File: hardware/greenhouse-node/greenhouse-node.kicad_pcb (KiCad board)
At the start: 2 copper layers, 90.2 x 69.8 mm, 49 parts, among them J1 Conn_01x12_Male, J2 Conn_01x02_Male, J3 Conn_01x02_Male, J4 Conn_01x02_Male, J5 Conn_01x04_Male, J6 RX_PinHeader_1x04_P2.54mm, J7 TX_PinHeader_1x04_P2.54mm, J8 Conn_01x02_Male, Q1 BC549C, Q2 BC549C, Q3 BC549C, Q4 IRF9530N, Q5 IRF530N, Q6 IRF9530N, Q7 IRF530N, Q8 BC549C, Q9 BC549C, U1 ATtiny84A-P, U2 L7805, U3 74HC595

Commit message: Tweak net positions
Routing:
- net /SR_RCLK: track 66.9 -> 68.4 mm
- net /SR_CLK: track 64.8 -> 65.6 mm
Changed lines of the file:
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@@
   (segment (start 139.446 92.837) (end 138.43 91.821) (width 0.25) (layer "F.Cu") (net 13))
   (segment (start 145.669 92.837) (end 139.446 92.837) (width 0.25) (layer "F.Cu") (net 13))
+  (segment (start 135.255 87.503) (end 135.255 72.0725) (width 0.25) (layer "B.Cu") (net 13))
+  (segment (start 134.511254 62.738) (end 137.541 62.738) (width 0.25) (layer "B.Cu") (net 13))
+  (segment (start 136.017 88.265) (end 135.255 87.503) (width 0.25) (layer "B.Cu") (net 13))
+  (segment (start 131.953 65.296254) (end 134.511254 62.738) (width 0.25) (layer "B.Cu") (net 13))
+  (segment (start 139.71 88.265) (end 136.017 88.265) (width 0.25) (layer "B.Cu") (net 13))
+  (segment (start 137.541 62.738) (end 140.723 59.556) (width 0.25) (layer "B.Cu") (net 13))
+  (segment (start 131.953 68.7705) (end 131.953 65.296254) (width 0.25) (layer "B.Cu") (net 13))
+  (segment (start 140.723 59.556) (end 140.723 58.022) (width 0.25) (layer "B.Cu") (net 13))
   (segment (start 135.255 72.0725) (end 131.953 68.7705) (width 0.25) (layer "B.Cu") (net 13))
-  (segment (start 131.953 65.296254) (end 134.511254 62.738) (width 0.25) (layer "B.Cu") (net 13))
-  (segment (start 137.541 62.738) (end 140.723 59.556) (width 0.25) (layer "B.Cu") (net 13))
-  (segment (start 138.557 88.265) (end 135.255 84.963) (width 0.25) (layer "B.Cu") (net 13))
-  (segment (start 131.953 68.7705) (end 131.953 65.296254) (width 0.25) (layer "B.Cu") (net 13))
-  (segment (start 135.255 84.963) (end 135.255 72.0725) (width 0.25) (layer "B.Cu") (net 13))
-  (segment (start 139.71 88.265) (end 138.557 88.265) (width 0.25) (layer "B.Cu") (net 13))
-  (segment (start 134.511254 62.738) (end 137.541 62.738) (width 0.25) (layer "B.Cu") (net 13))
-  (segment (start 140.723 59.556) (end 140.723 58.022) (width 0.25) (layer "B.Cu") (net 13))
+  (segment (start 139.319 94.107) (end 139.319 99.568) (width 0.25) (layer "B.Cu") (net 14))
+  (segment (start 132.09 90.805) (end 133.731 90.805) (width 0.25) (layer "B.Cu") (net 14))
+  (segment (start 145.542 101.473) (end 147.955 103.886) (width 0.25) (layer "B.Cu") (net 14))
   (segment (start 147.955 103.886) (end 147.955 105.41) (width 0.25) (layer "B.Cu") (net 14))
-  (segment (start 132.09 90.805) (end 133.731 90.805) (width 0.25) (layer "B.Cu") (net 14))
-  (segment (start 141.224 101.473) (end 145.542 101.473) (width 0.25) (layer "B.Cu") (net 14))
   (segment (start 135.723 59.476) (end 135.723 58.022) (width 0.25) (layer "B.Cu") (net 14))
-  (segment (start 133.731 90.805) (end 136.779 90.805) (width 0.25) (layer "B.Cu") (net 14))
   (segment (start 139.319 99.568) (end 141.224 101.473) (width 0.25) (layer "B.Cu") (net 14))
   (segment (start 130.683 64.516) (end 135.723 59.476) (width 0.25) (layer "B.Cu") (net 14))
   (segment (start 133.731 90.805) (end 133.731 72.415701) (width 0.25) (layer "B.Cu") (net 14))
   (segment (start 133.731 72.415701) (end 130.683 69.367701) (width 0.25) (layer "B.Cu") (net 14))
+  (segment (start 133.731 90.805) (end 136.017 90.805) (width 0.25) (layer "B.Cu") (net 14))
   (segment (start 130.683 69.367701) (end 130.683 64.516) (width 0.25) (layer "B.Cu") (net 14))
-  (segment (start 139.319 93.345) (end 139.319 99.568) (width 0.25) (layer "B.Cu") (net 14))
-  (segment (start 145.542 101.473) (end 147.955 103.886) (width 0.25) (layer "B.Cu") (net 14))
-  (segment (start 136.779 90.805) (end 139.319 93.345) (width 0.25) (layer "B.Cu") (net 14))
+  (segment (start 136.017 90.805) (end 139.319 94.107) (width 0.25) (layer "B.Cu") (net 14))
+  (segment (start 141.224 101.473) (end 145.542 101.473) (width 0.25) (layer "B.Cu") (net 14))
   (segment (start 144.907 90.805) (end 155.575 101.473) (width 0.25) (layer "F.Cu") (net 15))
   (segment (start 155.575 101.473) (end 155.575 105.41) (width 0.25) (layer "F.Cu") (net 15))
   (segment (start 139.71 90.805) (end 144.907 90.805) (width 0.25) (layer "F.Cu") (net 15))
+  (segment (start 134.493 72.263) (end 131.318 69.088) (width 0.25) (layer "B.Cu") (net 15))
+  (segment (start 138.223 59.389) (end 138.223 58.022) (width 0.25) (layer "B.Cu") (net 15))
+  (segment (start 131.318 69.088) (end 131.318 64.897) (width 0.25) (layer "B.Cu") (net 15))
+  (segment (start 131.318 64.897) (end 134.493 61.722) (width 0.25) (layer "B.Cu") (net 15))
   (segment (start 135.89 61.722) (end 138.223 59.389) (width 0.25) (layer "B.Cu") (net 15))
-  (segment (start 131.318 69.088) (end 131.318 64.897) (width 0.25) (layer "B.Cu") (net 15))
-  (segment (start 134.493 72.263) (end 131.318 69.088) (width 0.25) (layer "B.Cu") (net 15))
-  (segment (start 131.318 64.897) (end 134.493 61.722) (width 0.25) (layer "B.Cu") (net 15))
-  (segment (start 139.71 90.805) (end 138.557 90.805) (width 0.25) (layer "B.Cu") (net 15))
-  (segment (start 138.557 90.805) (end 134.493 86.741) (width 0.25) (layer "B.Cu") (net 15))
   (segment (start 134.493 61.722) (end 135.89 61.722) (width 0.25) (layer "B.Cu") (net 15))
-  (segment (start 134.493 86.741) (end 134.493 72.263) (width 0.25) (layer "B.Cu") (net 15))
-  (segment (start 138.223 59.389) (end 138.223 58.022) (width 0.25) (layer "B.Cu") (net 15))
+  (segment (start 137.287 90.805) (end 134.493 88.011) (width 0.25) (layer "B.Cu") (net 15))
+  (segment (start 139.71 90.805) (end 137.287 90.805) (width 0.25) (layer "B.Cu") (net 15))
+  (segment (start 134.493 88.011) (end 134.493 72.263) (width 0.25) (layer "B.Cu") (net 15))
   (segment (start 132.08 95.123) (end 133.35 93.853) (width 0.25) (layer "F.Cu") (net 16))
   (segment (start 133.35 93.853) (end 133.35 89.525) (width 0.25) (layer "F.Cu") (net 16))
+  (segment (start 140.208 97.028) (end 133.985 97.028) (width 0.25) (layer "F.Cu") (net 16))
+  (segment (start 133.985 97.028) (end 132.08 95.123) (width 0.25) (layer "F.Cu") (net 16))
   (segment (start 133.35 89.525) (end 132.09 88.265) (width 0.25) (layer "F.Cu") (net 16))
-  (segment (start 134.112 97.155) (end 132.08 95.123) (width 0.25) (layer "F.Cu") (net 16))
-  (segment (start 137.414 97.155) (end 134.112 97.155) (width 0.25) (layer "F.Cu") (net 16))
-  (segment (start 140.081 97.028) (end 137.541 97.028) (width 0.25) (layer "F.Cu") (net 16))
-  (segment (start 137.541 97.028) (end 137.414 97.155) (width 0.25) (layer "F.Cu") (net 16))
-  (via (at 140.081 97.028) (size 0.8) (drill 0.4) (layers "F.Cu" "B.Cu") (net 16))
+  (via (at 140.208 97.028) (size 0.8) (drill 0.4) (layers "F.Cu" "B.Cu") (net 16))
+  (segment (start 146.939 100.457) (end 150.495 104.013) (width 0.25) (layer "B.Cu") (net 16))
+  (segment (start 140.208 98.933) (end 141.732 100.457) (width 0.25) (layer "B.Cu") (net 16))
   (segment (start 141.732 100.457) (end 146.939 100.457) (width 0.25) (layer "B.Cu") (net 16))
-  (segment (start 140.081 97.028) (end 140.462 97.409) (width 0.25) (layer "B.Cu") (net 16))
-  (segment (start 140.462 99.187) (end 141.732 100.457) (width 0.25) (layer "B.Cu") (net 16))
-  (segment (start 140.462 97.409) (end 140.462 99.187) (width 0.25) (layer "B.Cu") (net 16))
+  (segment (start 140.208 97.028) (end 140.208 98.933) (width 0.25) (layer "B.Cu") (net 16))
   (segment (start 150.495 104.013) (end 150.495 105.41) (width 0.25) (layer "B.Cu") (net 16))
-  (segment (start 146.939 100.457) (end 150.495 104.013) (width 0.25) (layer "B.Cu") (net 16))
   (segment (start 139.446 94.996) (end 137.16 94.996) (width 0.25) (layer "F.Cu") (net 17))
   (segment (start 140.335 94.107) (end 139.446 94.996) (width 0.25) (layer "F.Cu") (net 17))

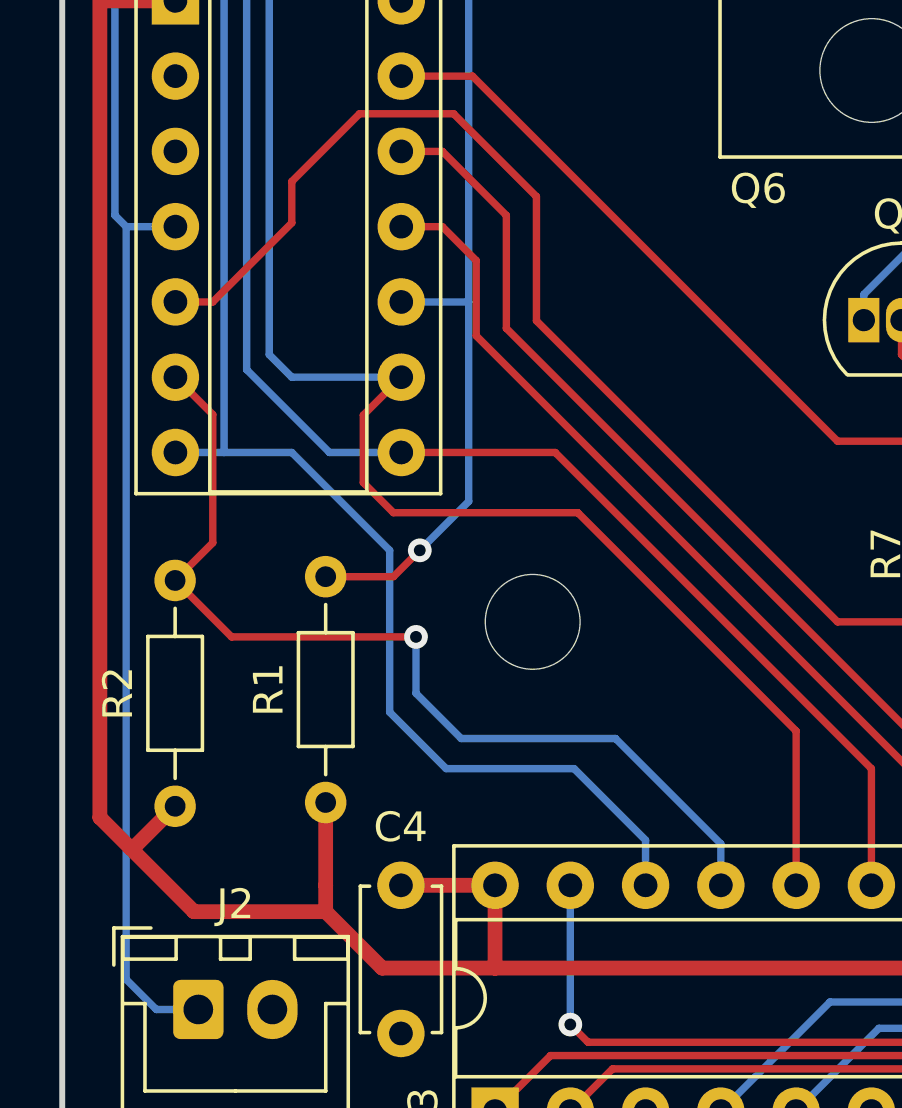
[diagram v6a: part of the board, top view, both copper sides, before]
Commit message: Removed some vias
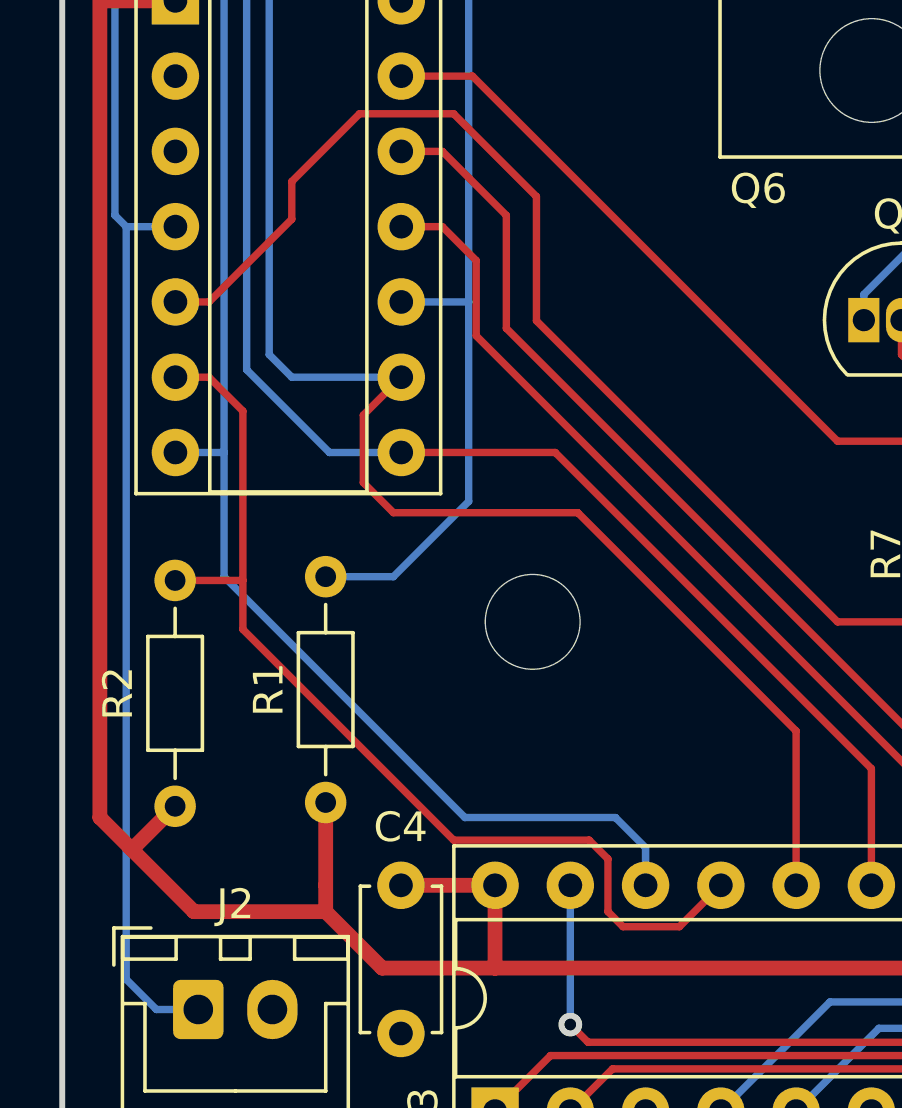
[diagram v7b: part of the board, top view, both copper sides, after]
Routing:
- net /SR_OE: track 32.5 -> 34.3 mm, vias 1 -> 0
- net /SR_SER: track 62.1 -> 61.2 mm
- net /OneWire: vias 1 -> 0
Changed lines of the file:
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@@
   (segment (start 161.544 88.9) (end 157.988 88.9) (width 0.25) (layer "F.Cu") (net 8))
   (segment (start 157.988 88.9) (end 156.591 87.503) (width 0.25) (layer "F.Cu") (net 8))
+  (segment (start 136.017 82.931) (end 133.223 85.725) (width 0.25) (layer "F.Cu") (net 9))
+  (segment (start 133.223 85.725) (end 132.09 85.725) (width 0.25) (layer "F.Cu") (net 9))
+  (segment (start 178.435 98.171) (end 173.355 98.171) (width 0.25) (layer "F.Cu") (net 9))
+  (segment (start 154.432 96.52) (end 144.272 86.36) (width 0.25) (layer "F.Cu") (net 9))
+  (segment (start 173.355 98.171) (end 171.704 96.52) (width 0.25) (layer "F.Cu") (net 9))
   (segment (start 171.704 96.52) (end 154.432 96.52) (width 0.25) (layer "F.Cu") (net 9))
   (segment (start 141.478 79.375) (end 138.303 79.375) (width 0.25) (layer "F.Cu") (net 9))
+  (segment (start 138.303 79.375) (end 136.017 81.661) (width 0.25) (layer "F.Cu") (net 9))
   (segment (start 144.272 82.169) (end 141.478 79.375) (width 0.25) (layer "F.Cu") (net 9))
-  (segment (start 138.303 79.375) (end 136.017 81.661) (width 0.25) (layer "F.Cu") (net 9))
-  (segment (start 136.017 83.058) (end 133.35 85.725) (width 0.25) (layer "F.Cu") (net 9))
-  (segment (start 178.435 98.171) (end 173.355 98.171) (width 0.25) (layer "F.Cu") (net 9))
-  (segment (start 133.35 85.725) (end 132.09 85.725) (width 0.25) (layer "F.Cu") (net 9))
+  (segment (start 136.017 81.661) (end 136.017 82.931) (width 0.25) (layer "F.Cu") (net 9))
   (segment (start 144.272 86.36) (end 144.272 82.169) (width 0.25) (layer "F.Cu") (net 9))
-  (segment (start 173.355 98.171) (end 171.704 96.52) (width 0.25) (layer "F.Cu") (net 9))
-  (segment (start 136.017 81.661) (end 136.017 83.058) (width 0.25) (layer "F.Cu") (net 9))
-  (segment (start 154.432 96.52) (end 144.272 86.36) (width 0.25) (layer "F.Cu") (net 9))
   (segment (start 167.0679 55.6492) (end 167.0679 61.255) (width 2) (layer "F.Cu") (net 10))
   (segment (start 184.277 84.074) (end 185.42 85.217) (width 0.25) (layer "F.Cu") (net 10))
@@
   (segment (start 140.723 59.556) (end 140.723 58.022) (width 0.25) (layer "B.Cu") (net 13))
   (segment (start 135.255 72.0725) (end 131.953 68.7705) (width 0.25) (layer "B.Cu") (net 13))
-  (segment (start 139.319 94.107) (end 139.319 99.568) (width 0.25) (layer "B.Cu") (net 14))
   (segment (start 132.09 90.805) (end 133.731 90.805) (width 0.25) (layer "B.Cu") (net 14))
-  (segment (start 145.542 101.473) (end 147.955 103.886) (width 0.25) (layer "B.Cu") (net 14))
-  (segment (start 147.955 103.886) (end 147.955 105.41) (width 0.25) (layer "B.Cu") (net 14))
+  (segment (start 141.859 103.124) (end 146.939 103.124) (width 0.25) (layer "B.Cu") (net 14))
+  (segment (start 133.731 94.996) (end 141.859 103.124) (width 0.25) (layer "B.Cu") (net 14))
   (segment (start 135.723 59.476) (end 135.723 58.022) (width 0.25) (layer "B.Cu") (net 14))
-  (segment (start 139.319 99.568) (end 141.224 101.473) (width 0.25) (layer "B.Cu") (net 14))
+  (segment (start 133.731 90.805) (end 133.731 94.996) (width 0.25) (layer "B.Cu") (net 14))
+  (segment (start 146.939 103.124) (end 147.955 104.14) (width 0.25) (layer "B.Cu") (net 14))
   (segment (start 130.683 64.516) (end 135.723 59.476) (width 0.25) (layer "B.Cu") (net 14))
   (segment (start 133.731 90.805) (end 133.731 72.415701) (width 0.25) (layer "B.Cu") (net 14))
   (segment (start 133.731 72.415701) (end 130.683 69.367701) (width 0.25) (layer "B.Cu") (net 14))
-  (segment (start 133.731 90.805) (end 136.017 90.805) (width 0.25) (layer "B.Cu") (net 14))
   (segment (start 130.683 69.367701) (end 130.683 64.516) (width 0.25) (layer "B.Cu") (net 14))
-  (segment (start 136.017 90.805) (end 139.319 94.107) (width 0.25) (layer "B.Cu") (net 14))
-  (segment (start 141.224 101.473) (end 145.542 101.473) (width 0.25) (layer "B.Cu") (net 14))
+  (segment (start 147.955 104.14) (end 147.955 105.41) (width 0.25) (layer "B.Cu") (net 14))
   (segment (start 144.907 90.805) (end 155.575 101.473) (width 0.25) (layer "F.Cu") (net 15))
   (segment (start 155.575 101.473) (end 155.575 105.41) (width 0.25) (layer "F.Cu") (net 15))
@@
   (segment (start 139.71 90.805) (end 137.287 90.805) (width 0.25) (layer "B.Cu") (net 15))
   (segment (start 134.493 88.011) (end 134.493 72.263) (width 0.25) (layer "B.Cu") (net 15))
-  (segment (start 132.08 95.123) (end 133.35 93.853) (width 0.25) (layer "F.Cu") (net 16))
-  (segment (start 133.35 93.853) (end 133.35 89.525) (width 0.25) (layer "F.Cu") (net 16))
-  (segment (start 140.208 97.028) (end 133.985 97.028) (width 0.25) (layer "F.Cu") (net 16))
-  (segment (start 133.985 97.028) (end 132.08 95.123) (width 0.25) (layer "F.Cu") (net 16))
-  (segment (start 133.35 89.525) (end 132.09 88.265) (width 0.25) (layer "F.Cu") (net 16))
-  (via (at 140.208 97.028) (size 0.8) (drill 0.4) (layers "F.Cu" "B.Cu") (net 16))
-  (segment (start 146.939 100.457) (end 150.495 104.013) (width 0.25) (layer "B.Cu") (net 16))
-  (segment (start 140.208 98.933) (end 141.732 100.457) (width 0.25) (layer "B.Cu") (net 16))
-  (segment (start 141.732 100.457) (end 146.939 100.457) (width 0.25) (layer "B.Cu") (net 16))
-  (segment (start 140.208 97.028) (end 140.208 98.933) (width 0.25) (layer "B.Cu") (net 16))
-  (segment (start 150.495 104.013) (end 150.495 105.41) (width 0.25) (layer "B.Cu") (net 16))
-  (segment (start 139.446 94.996) (end 137.16 94.996) (width 0.25) (layer "F.Cu") (net 17))
-  (segment (start 140.335 94.107) (end 139.446 94.996) (width 0.25) (layer "F.Cu") (net 17))
-  (via (at 140.335 94.107) (size 0.8) (drill 0.4) (layers "F.Cu" "B.Cu") (net 17))
+  (segment (start 132.09 88.265) (end 133.223 88.265) (width 0.25) (layer "F.Cu") (net 16))
+  (segment (start 134.366 96.774) (end 141.478 103.886) (width 0.25) (layer "F.Cu") (net 16))
+  (segment (start 134.366 95.123) (end 134.366 96.774) (width 0.25) (layer "F.Cu") (net 16))
+  (segment (start 146.685 104.521) (end 146.685 106.299) (width 0.25) (layer "F.Cu") (net 16))
+  (segment (start 146.05 103.886) (end 146.685 104.521) (width 0.25) (layer "F.Cu") (net 16))
+  (segment (start 133.223 88.265) (end 134.366 89.408) (width 0.25) (layer "F.Cu") (net 16))
+  (segment (start 146.685 106.299) (end 147.193 106.807) (width 0.25) (layer "F.Cu") (net 16))
+  (segment (start 141.478 103.886) (end 146.05 103.886) (width 0.25) (layer "F.Cu") (net 16))
+  (segment (start 149.098 106.807) (end 150.495 105.41) (width 0.25) (layer "F.Cu") (net 16))
+  (segment (start 134.366 95.123) (end 132.08 95.123) (width 0.25) (layer "F.Cu") (net 16))
+  (segment (start 134.366 89.408) (end 134.366 95.123) (width 0.25) (layer "F.Cu") (net 16))
+  (segment (start 147.193 106.807) (end 149.098 106.807) (width 0.25) (layer "F.Cu") (net 16))
   (segment (start 139.7 50.78) (end 139.7 54.102) (width 0.25) (layer "B.Cu") (net 17))
   (segment (start 147.32 54.102) (end 139.7 54.102) (width 0.25) (layer "B.Cu") (net 17))
+  (segment (start 141.986 92.456) (end 139.446 94.996) (width 0.25) (layer "B.Cu") (net 17))
+  (segment (start 141.986 85.725) (end 141.986 92.456) (width 0.25) (layer "B.Cu") (net 17))
   (segment (start 154.94 52.07) (end 152.908 54.102) (width 0.25) (layer "B.Cu") (net 17))
   (segment (start 139.71 85.725) (end 141.986 85.725) (width 0.25) (layer "B.Cu") (net 17))
@@
   (segment (start 154.94 50.78) (end 154.94 52.07) (width 0.25) (layer "B.Cu") (net 17))
   (segment (start 144.018 54.737) (end 144.018 59.944) (width 0.25) (layer "B.Cu") (net 17))
-  (segment (start 141.986 92.456) (end 141.986 85.725) (width 0.25) (layer "B.Cu") (net 17))
   (segment (start 152.908 54.102) (end 147.32 54.102) (width 0.25) (layer "B.Cu") (net 17))
   (segment (start 140.335 71.755) (end 141.986 73.406) (width 0.25) (layer "B.Cu") (net 17))
@@
   (segment (start 147.32 50.78) (end 147.32 54.102) (width 0.25) (layer "B.Cu") (net 17))
   (segment (start 134.8205 54.102) (end 139.7 54.102) (width 0.25) (layer "B.Cu") (net 17))
-  (segment (start 140.335 94.107) (end 141.986 92.456) (width 0.25) (layer "B.Cu") (net 17))
+  (segment (start 139.446 94.996) (end 137.16 94.996) (width 0.25) (layer "B.Cu") (net 17))
   (segment (start 143.256 82.804) (end 141.097 80.645) (width 0.25) (layer "F.Cu") (net 18))
   (segment (start 141.097 80.645) (end 139.71 80.645) (width 0.25) (layer "F.Cu") (net 18))
